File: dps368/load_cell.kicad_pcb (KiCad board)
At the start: 2 copper layers, 6.6 x 5.8 mm, 6 parts, among them J1 Conn_01x05_Female, U1 DPS368XTSA1

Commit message: goddamn it
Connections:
- C1 pad 1: +3V3 -> GND
- C1 pad 2: Net-(C1-Pad2) -> +3V3
- C2 pad 1: Net-(C2-Pad1) -> GND
- U1 pad 6: Net-(C2-Pad1) -> +3V3
- U1 pad 8: Net-(C1-Pad2) -> +3V3
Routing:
- net +3V3: track 10.8 -> 14.7 mm
- net GND: track 6.71 -> 9.58 mm
- net Net-(C2-Pad1): track 2.66 -> 0.00 mm
- net Net-(C1-Pad2): track 1.29 -> 0.00 mm

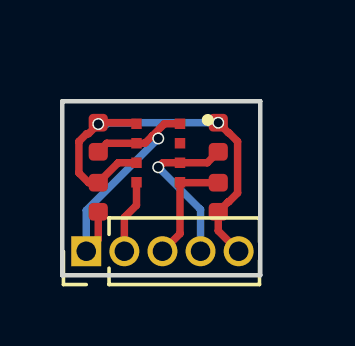
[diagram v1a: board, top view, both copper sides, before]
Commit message: 7mm diameter sensor
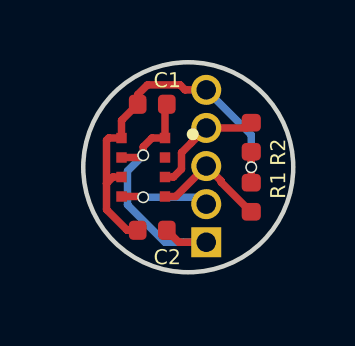
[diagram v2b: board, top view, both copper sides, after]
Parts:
- J1: moved to B.Cu
- moved J1 4.01 mm to (142.6, 96.5), turned to 0 degrees
- moved C1 2.11 mm to (140.8, 91.9), turned to 180 degrees
- moved C2 2.11 mm to (140.8, 96.1), turned to 180 degrees
- moved R1 1.10 mm to (144.1, 95.0), turned to 270 degrees
- moved R2 1.10 mm to (144.1, 93.0), turned to 90 degrees
- moved U1 0.69 mm to (140.5, 94.0)
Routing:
- net /sdi: track 5.60 -> 3.94 mm, vias 1 -> 0
- net +3V3: track 14.7 -> 13.1 mm, vias 2 -> 1
- net /sdo: track 2.47 -> 2.93 mm, vias 0 -> 1
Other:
- board size 6.6 x 5.8 mm -> 7 x 7 mm
